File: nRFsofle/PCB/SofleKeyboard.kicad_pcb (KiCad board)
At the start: 2 copper layers, 143.9 x 113.6 mm, 112 parts, among them J1 LED, J2 4PIN, J3 OLED, J4 key leds, J5 backlight sel, J6 indicator bypass, J7 JST_Micro_2, J8 OLED, P1 i2c_pin, P2 i2c_pin, SW1 SW_PUSH-MX_W_LED, SW10 SW_PUSH-MX_W_LED, SW11 SW_PUSH-MX_W_LED, SW12 SW_PUSH-MX_W_LED, SW13 SW_PUSH-MX_W_LED, SW14 SW_PUSH-MX_W_LED, SW15 SW_PUSH-MX_W_LED, SW16 SW_PUSH-MX_W_LED, SW17 SW_PUSH-MX_W_LED, SW18 SW_PUSH-MX_W_LED, SW19 SW_PUSH-MX_W_LED, SW2 SW_PUSH-MX_W_LED, SW20 SW_PUSH-MX_W_LED, SW21 SW_PUSH-MX_W_LED, SW22 SW_PUSH-MX_W_LED, SW23 SW_PUSH-MX_W_LED, SW24 SW_PUSH-MX_W_LED, SW25 Rotary_Encoder_Switch, SW26 SW_PUSH-MX_W_LED, SW27 SW_PUSH-MX_W_LED, SW28 SW_PUSH-MX_W_LED, SW29 SW_PUSH-MX_W_LED, SW3 SW_PUSH-MX_W_LED, SW30 SW_PUSH-MX_W_LED, SW31 SPDT_Switch, SW4 SW_PUSH-MX_W_LED, SW5 SW_PUSH-MX_W_LED, SW6 SW_PUSH-MX_W_LED, SW7 SW_PUSH-MX_W_LED, SW8 SW_PUSH-MX_W_LED, SW9 SW_PUSH-MX_W_LED, U1 nRFMicro

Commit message: Implemented the schematic to add fingerprint sensor
The implemented circuit is duplicated to put the circuit in both layers,
so the board can be printed for both sides of the keyboard.
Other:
- board text added: "https://github.com/classOpenGL/SofleKeyboard"
- board text removed: "https://josefadamcik.github.io/SofleKeyboard/"

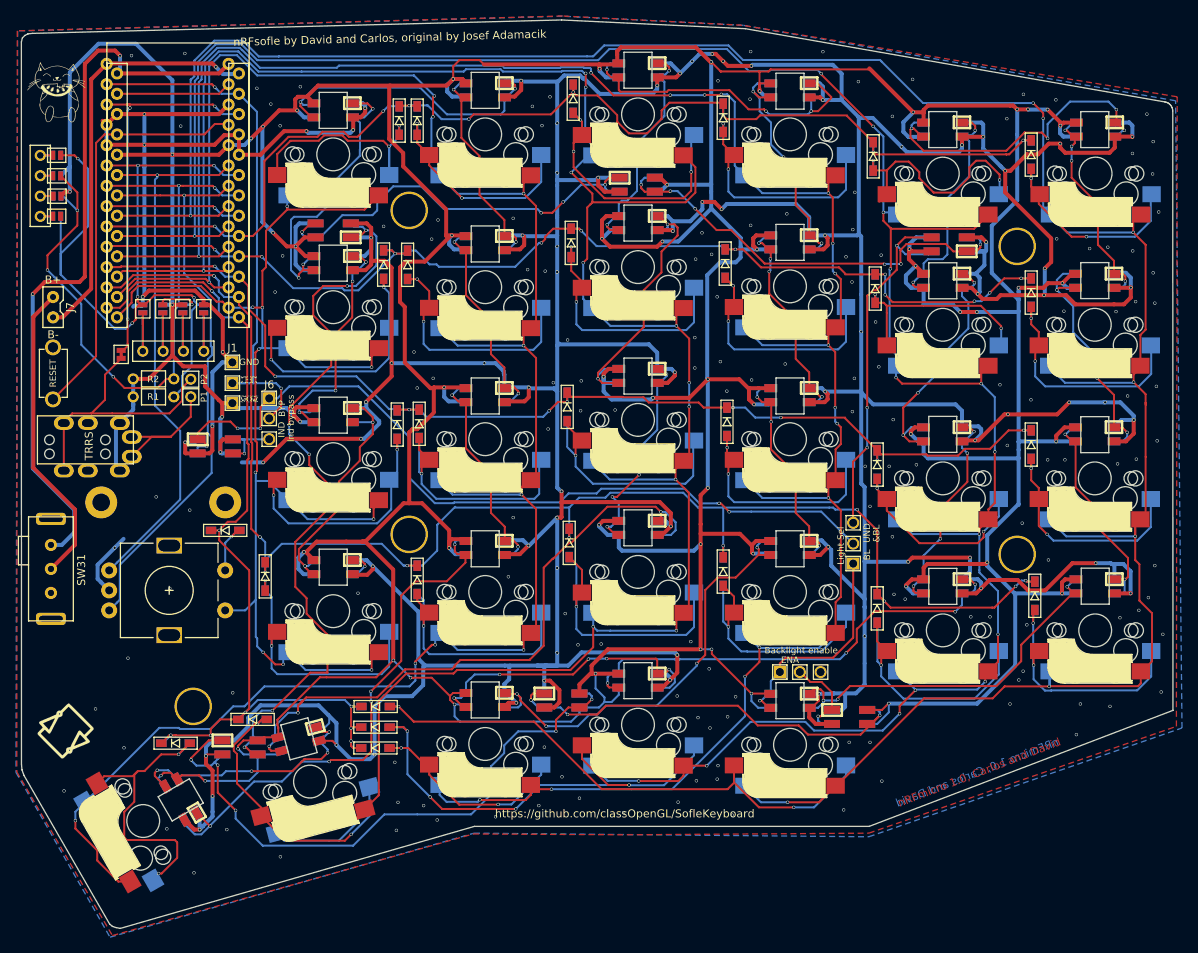
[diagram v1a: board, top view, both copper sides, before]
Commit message: Generated the PCB to add fingerprint sensor to the keyboard
In order to add this new feature, a microcontroller was added.
It is duplicated because this board can be used as left and
right sides of the keyboard, so only one of the sides should
be soldered.

The Atmega microcontroller reads the fingerprint sensor using
UART protocol while the nRFmicro reads the Arduino fingerprint
sensor read data using I2C sensor. An additional wire was added
between the Atmega and the nRFmicro to the Atmega be able to
interrupt the nRFmicro every time the fingerprint sensor detects a
finger.
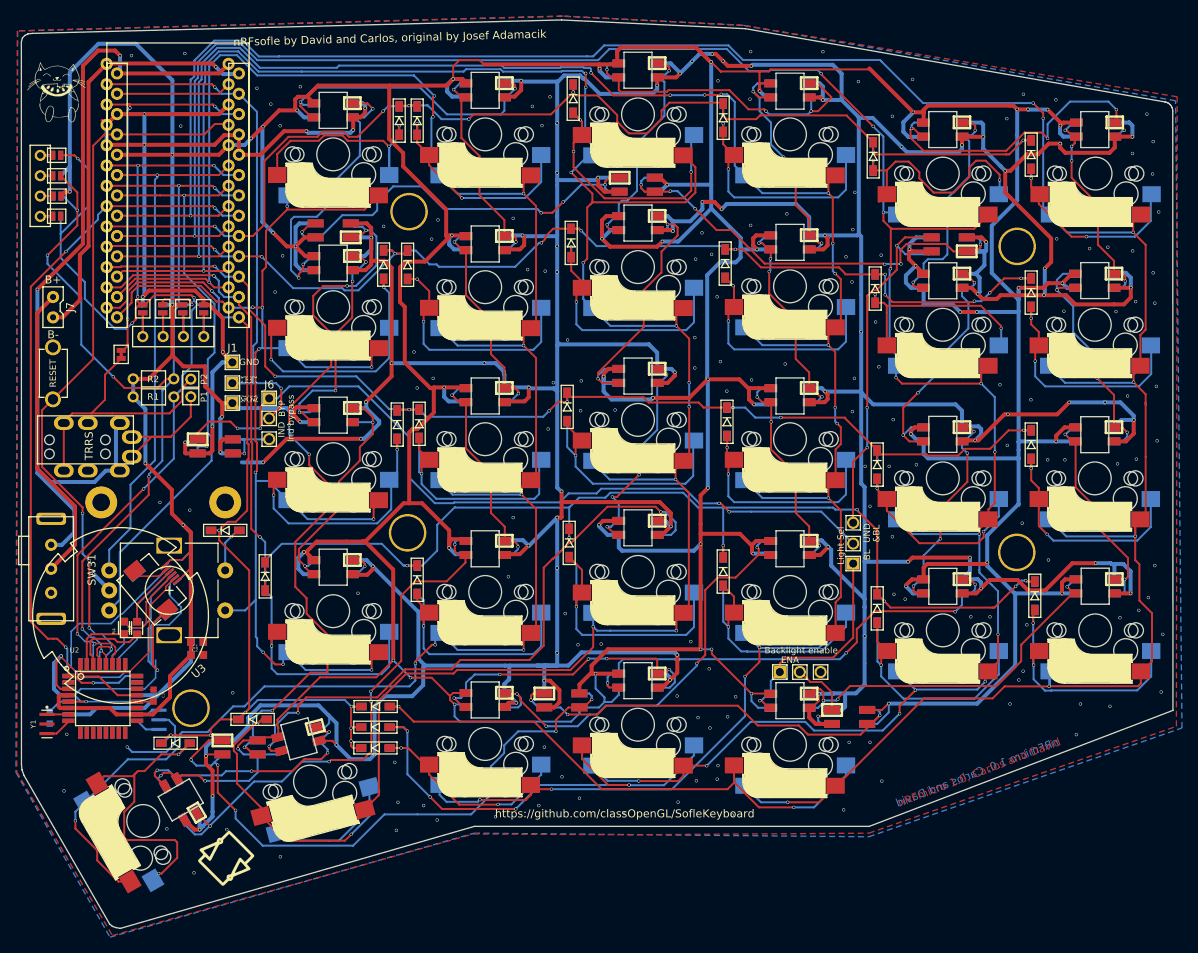
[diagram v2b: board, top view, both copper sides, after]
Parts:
- added C1: 1uF, Additions:1uF, F.Cu at (103.5, 112.6)
- added C2: 1uF, Additions:1uF, F.Cu at (103.5, 110.9)
- added C3: 100nF, Additions:100nF, F.Cu at (98.0, 117.7)
- added C4: 1uF, Additions:1uF, B.Cu at (103.5, 110.9)
- added C5: 1uF, Additions:1uF, B.Cu at (103.5, 112.6)
- added C6: 100nF, Additions:100nF, B.Cu at (85.1, 120.4)
- added R3: 1k, Additions:1k, F.Cu at (96.0, 109.2)
- added R4: 1k, Additions:1k, F.Cu at (94.3, 109.2)
- added R5: 1k, Additions:1k, B.Cu at (94.3, 109.2)
- added R6: 1k, Additions:1k, B.Cu at (96.0, 109.2)
- added U2: ATMEGA328P-AU, Additions:QFP80P900X900X120-32N, F.Cu at (91.7, 118.0)
- added U3: R502-B, Additions:R502-B, F.Cu at (102.1, 117.4)
- added U4: ATMEGA328P-AU, Additions:QFP80P900X900X120-32N, B.Cu at (91.7, 118.0)
- added U5: R502-B, Additions:R502-B, B.Cu at (85.8, 98.0)
- added Y1: CSTCE8M00G52-R0, Additions:OSC_CSTCE8M00G52-R0, F.Cu at (84.7, 121.2)
- added Y2: CSTCE8M00G52-R0, Additions:OSC_CSTCE8M00G52-R0, B.Cu at (98.7, 120.7)
- moved Ref** 25.6 mm to (107.1, 137.9)
- moved Ref** 25.5 mm to (106.9, 138.0)
- moved J3 1.83 mm to (96.7, 72.8)
- moved TH3 0.43 mm to (130.2, 57.4)
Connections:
- J2 pad 1: VCC -> B+
- U1 pad 8: Net-(U1-Pad8) -> FP_INT
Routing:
- net VCC: track 968.5 -> 1068.5 mm, vias 58 -> 60
- net FP_INT: track 0.00 -> 91.8 mm, vias 0 -> 5
- net GND: track 962.2 -> 1053.1 mm, vias 230 -> 231
- net SCL: track 91.8 -> 135.5 mm, vias 6 -> 9
- net RESET: track 52.2 -> 94.3 mm, vias 0 -> 4
- net SDA: track 98.7 -> 138.6 mm, vias 6 -> 9
- net Net-(U4-Pad32): track 0.00 -> 28.2 mm
- net Net-(U2-Pad32): track 0.00 -> 21.2 mm
- net Net-(U1-Pad8): track 17.0 -> 0.00 mm, vias 1 -> 0
- net B+: track 91.7 -> 104.7 mm
- net Net-(R4-Pad2): track 0.00 -> 10.8 mm
- net Net-(R5-Pad2): track 0.00 -> 10.7 mm
- net Net-(R3-Pad1): track 0.00 -> 9.52 mm
- net Net-(R4-Pad1): track 0.00 -> 8.12 mm
- net Net-(R3-Pad2): track 0.00 -> 7.92 mm
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
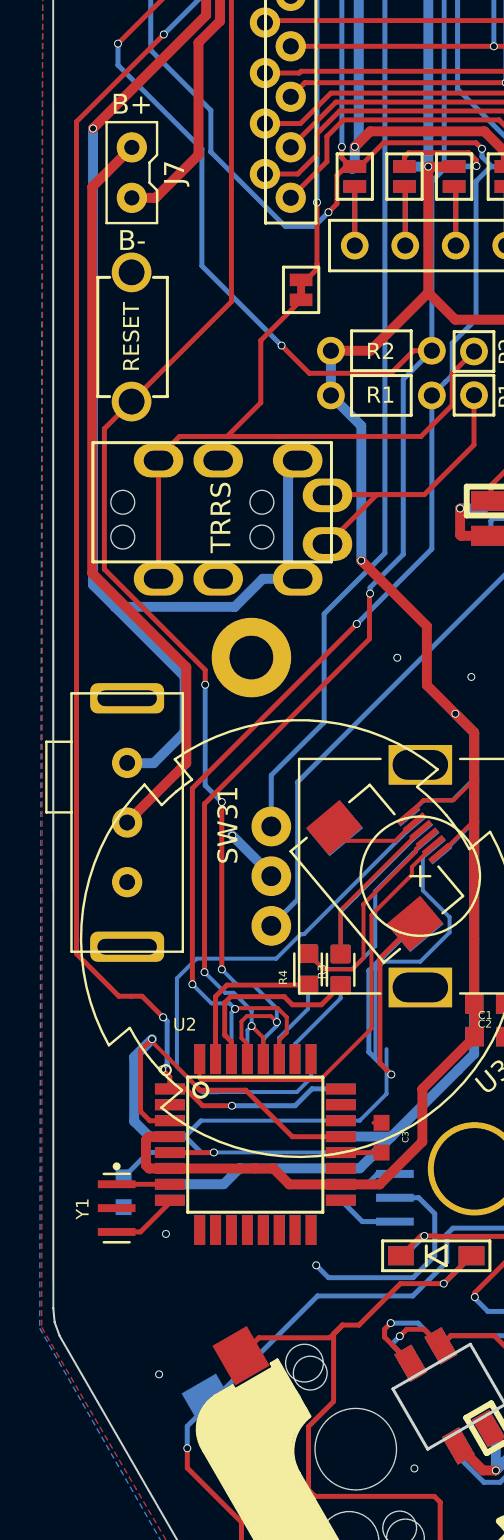
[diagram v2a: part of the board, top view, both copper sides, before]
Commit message: Added SPI programmer port interface
Pinout of this port is equal to the used by Arduino Nano
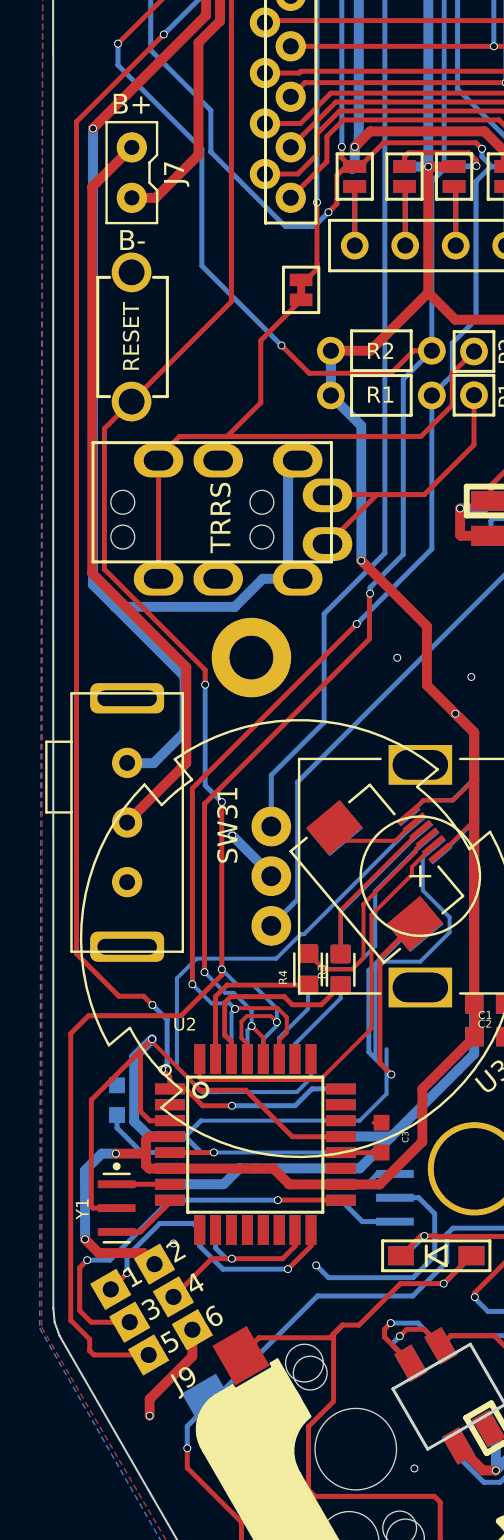
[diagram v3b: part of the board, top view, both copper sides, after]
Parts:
- added J9: SPI_PADS, Additions:SPI_PADS, F.Cu at (83.2, 123.1)
- moved C6 4.64 mm to (84.7, 115.8), turned to 270 degrees
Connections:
- U2 pad 15: Net-(U2-Pad15) -> MOSI
- U2 pad 16: Net-(U2-Pad16) -> MISO
- U2 pad 17: Net-(U2-Pad17) -> SCK
- U4 pad 15: Net-(U4-Pad15) -> MOSI
- U4 pad 16: Net-(U4-Pad16) -> MISO
- U4 pad 17: Net-(U4-Pad17) -> SCK
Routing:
- net RESET: track 94.3 -> 123.0 mm
- net SCK: track 0.00 -> 19.5 mm, vias 0 -> 2
- net GND: track 1053.1 -> 1069.3 mm
- net MISO: track 0.00 -> 14.7 mm, vias 0 -> 2
- net VCC: track 1068.5 -> 1079.4 mm, vias 60 -> 62
- net MOSI: track 0.00 -> 9.93 mm, vias 0 -> 1
- net Net-(C6-Pad2): track 2.85 -> 3.82 mm

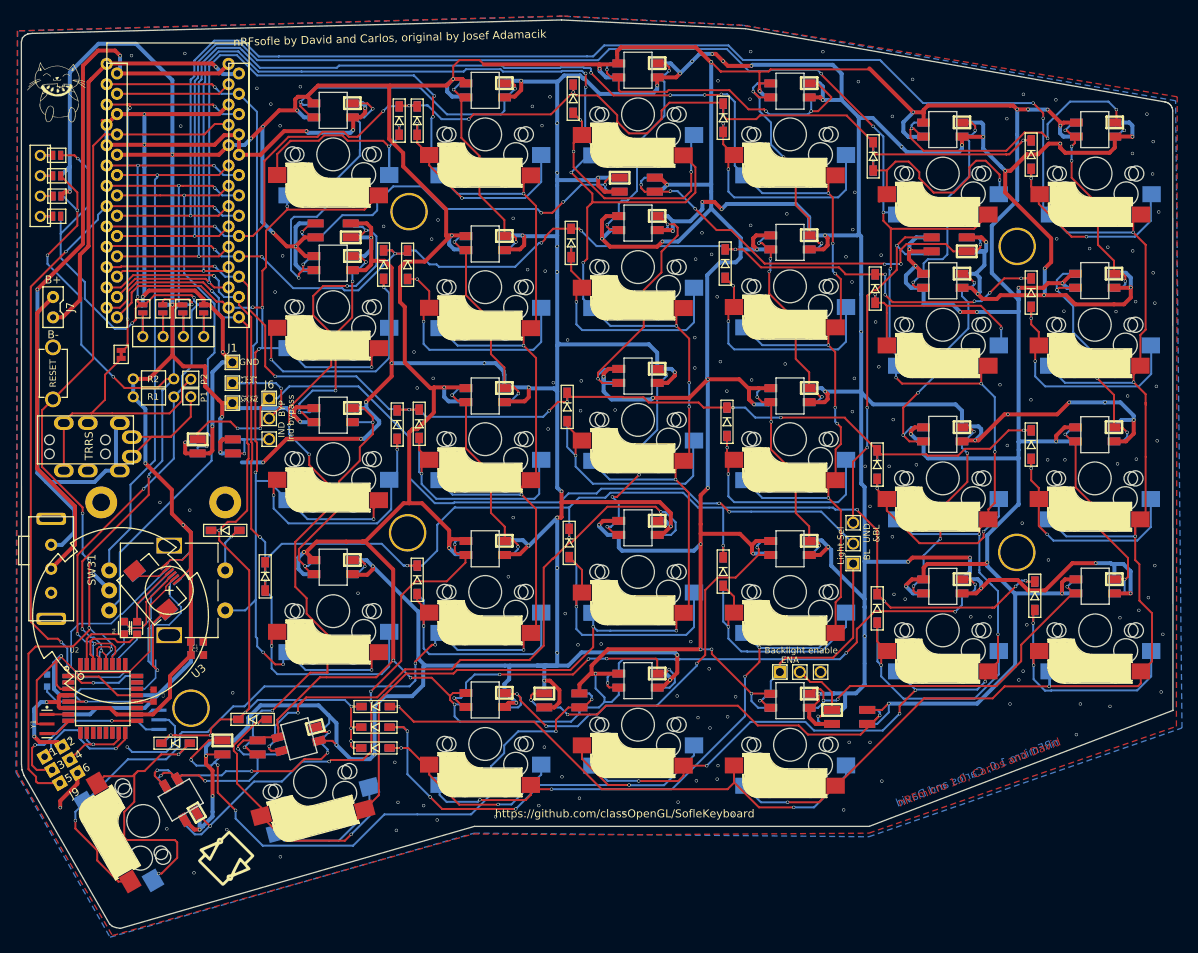
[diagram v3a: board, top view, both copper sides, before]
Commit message: Added 3D models for keyboard building
Several models created with FreeCAD were added in order to
be able to build the keyboard. These models are:

 * Fitgerprint support (bottom)
 * Fingerprint support (top)
 * Plate spacer (should be used in top plate)

Both fingerprint supports are used together to keep the
sensor on the top plate.
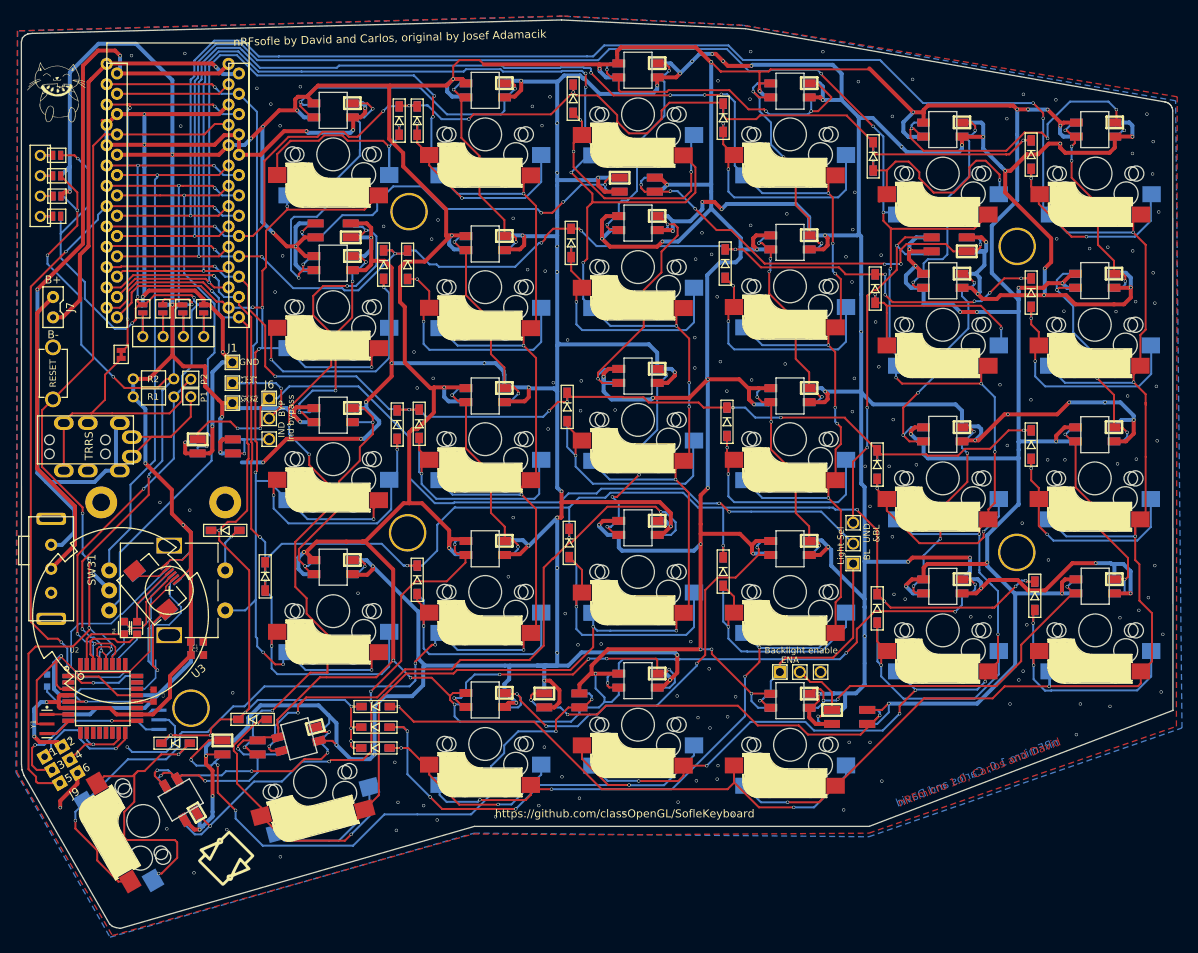
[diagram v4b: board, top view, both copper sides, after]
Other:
- net class Default removed
- net class GND removed
- net class VCC removed
